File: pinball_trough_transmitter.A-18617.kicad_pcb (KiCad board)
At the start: 2 copper layers, 162.6 x 88.5 mm, 16 parts, among them J1 Conn_01x09_Male, J2 Conn_01x09_Male, Q1 SFH460, Q2 SFH460, Q3 SFH460, Q4 SFH460, Q5 SFH460, Q6 SFH460, Q7 SFH460

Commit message: Minor adjustments
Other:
- outline, holes or cut-outs redrawn
- board text added: "Rev: v1.13"
- board text removed: "Rev: v1.12"
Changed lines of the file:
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@@
   (general
     (thickness 1.6)
-    (drawings 31)
+    (drawings 39)
     (tracks 0)
     (zones 0)
@@
   (page A4)
   (title_block
-    (rev v1.12)
+    (rev v1.13)
   )
   (layers
@@
     )
   )
-  (gr_text "Rev: v1.12" (at 68.81 81.1) (layer F.SilkS)
+  (gr_line (start 210 45.72) (end 210 53.72) (layer Edge.Cuts) (width 0.15))
+  (gr_line (start 180 45.72) (end 180 53.72) (layer Edge.Cuts) (width 0.15))
+  (gr_line (start 130 45.72) (end 130 53.72) (layer Edge.Cuts) (width 0.15))
+  (gr_line (start 100 45.72) (end 100 53.72) (layer Edge.Cuts) (width 0.15))
+  (gr_line (start 130 45.72) (end 180 45.72) (layer Edge.Cuts) (width 0.15))
+  (gr_line (start 100 53.72) (end 130 53.72) (layer Edge.Cuts) (width 0.15))
+  (gr_line (start 180 53.72) (end 210 53.72) (layer Edge.Cuts) (width 0.15))
+  (gr_line (start 210 45.72) (end 229.87 45.72) (layer Edge.Cuts) (width 0.15))
+  (gr_text "Rev: v1.13" (at 68.81 81.1) (layer F.SilkS)
     (effects (font (size 1.5 1.5) (thickness 0.3)) (justify left))
   )
@@
   (gr_line (start 73.02 54.51) (end 73.02 62.13) (layer F.SilkS) (width 0.15))
   (gr_line (start 80.64 54.51) (end 73.02 54.51) (layer F.SilkS) (width 0.15))
-  (gr_circle (center 144.407 57.277) (end 145.894898 58.547) (layer Edge.Cuts) (width 0.15))
+  (gr_circle (center 144.907 57.277) (end 146.394898 58.547) (layer Edge.Cuts) (width 0.15))
   (gr_circle (center 90.424 57.785) (end 91.911898 59.055) (layer Edge.Cuts) (width 0.15))
-  (gr_circle (center 144.407 63.627) (end 145.894898 64.897) (layer Edge.Cuts) (width 0.15))
+  (gr_circle (center 144.907 63.627) (end 146.394898 64.897) (layer Edge.Cuts) (width 0.15))
   (gr_circle (center 199.144 69.85) (end 200.631898 71.12) (layer Edge.Cuts) (width 0.15))
   (gr_line (start 67.277387 134.230068) (end 229.837387 134.230068) (layer Edge.Cuts) (width 0.15))
@@
   (gr_line (start 229.87 59.69) (end 213.36 83.82) (layer Edge.Cuts) (width 0.15))
   (gr_line (start 229.87 45.72) (end 229.87 59.69) (layer Edge.Cuts) (width 0.15))
-  (gr_line (start 67.31 45.72) (end 229.87 45.72) (layer Edge.Cuts) (width 0.15))
+  (gr_line (start 67.31 45.72) (end 100 45.72) (layer Edge.Cuts) (width 0.15))
   (gr_line (start 67.31 83.82) (end 213.36 83.82) (layer Edge.Cuts) (width 0.15))
 )

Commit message: Final adjustments (hopefully)
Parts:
- removed J2: Conn_01x09_Male, Connector_Molex:Molex_KK-254_AE-6410-09A_1x09_P2.54mm_Vertical
- removed Q1, Q2, Q3, Q4, Q5, Q6, Q7: SFH460, LED_THT:LED_D5.0mm_IRBlack
- J1: footprint Connector_Molex:Molex_KK-254_AE-6410-09A_1x09_P2.54mm_Vertical -> Connector_PinHeader_2_54:PinHeader_1x09_P2.54mm_Horizontal
- moved J1 1.42 mm to (122.6, 75.6), turned to 270 degrees
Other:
- board size 162.6 x 88.5 mm -> 162.6 x 38.1 mm
- board text added: "Rev: v1.14"
- board text removed: "Rev: v1.13"

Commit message: Manually flip board
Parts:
- moved D1 444.5 mm to (-222.2, 55.7)
- moved D2 424.4 mm to (-212.2, 74.8)
- moved D3 370.2 mm to (-185.1, 71.8)
- moved D4 316.1 mm to (-158.0, 68.7)
- moved D5 262.0 mm to (-131.0, 65.7)
- moved J1 245.1 mm to (-122.6, 75.6)
- moved D6 207.8 mm to (-103.9, 62.6)
- moved D7 153.7 mm to (-76.8, 59.6)
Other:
- outline, holes or cut-outs redrawn
- board text added: "Rev: v1.15"
- board text removed: "Rev: v1.14"

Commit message: Programmatically flip instead
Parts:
- D1, D2, D3, D4, D5, D6, D7, J1: moved to B.Cu
- moved J1 292.5 mm to (168.9, 100.3)
- moved D1 292.3 mm to (69.2, 77.9)
- moved D2 292.3 mm to (79.3, 97.1)
- moved D3 292.3 mm to (106.4, 94.0)
- moved D4 292.3 mm to (133.4, 91.0)
- moved D5 292.3 mm to (160.5, 87.9)
- moved D6 292.3 mm to (187.6, 84.9)
- moved D7 292.3 mm to (214.6, 81.8)
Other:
- board text added: "Rev: v1.16"
- board text removed: "Rev: v1.15"

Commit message: Almost there
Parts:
- moved D1 149.5 mm to (218.4, 87.5)
- moved D7 141.9 mm to (73.0, 91.3)
- moved D2 129.4 mm to (208.4, 106.6)
- moved D6 88.0 mm to (100.1, 94.4)
- moved D3 75.6 mm to (181.3, 103.5)
- moved J1 71.1 mm to (98.4, 109.9)
- moved D5 34.7 mm to (127.2, 97.4)
- moved D4 22.9 mm to (154.2, 100.5)
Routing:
- net Net-(D1-Pad1): track 0.00 -> 187.3 mm
- net Net-(D1-Pad2): track 0.00 -> 119.6 mm
- net Net-(D2-Pad2): track 0.00 -> 102.4 mm
- net Net-(D3-Pad2): track 0.00 -> 77.5 mm
- net Net-(D4-Pad2): track 0.00 -> 52.1 mm
- net Net-(D7-Pad2): track 0.00 -> 35.1 mm
- net Net-(D5-Pad2): track 0.00 -> 28.9 mm
- net Net-(D6-Pad2): track 0.00 -> 13.3 mm
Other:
- outline, holes or cut-outs redrawn
- board text added: "(4 ball)"
- board text added: "(6 ball)"
- board text added: "(board)"
- board text added: "5768-14121-02"
- board text added: "A-18617"
- board text added: "A-18617-1"
- board text added: "BALL1"
- board text added: "BALL2"
- board text added: "BALL3"
- board text added: "BALL4"
- board text added: "BALL5"
- board text added: "BALL6"
- board text added: "COM"
- board text added: "COMPONENT SIDE"
- board text added: "JAM"
- board text added: "KEY"
- board text added: "Rev: v1.17"
- board text removed: "Rev: v1.16"

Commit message: I think... we're done
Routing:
- net Net-(D5-Pad2): track 28.9 -> 30.7 mm
- net Net-(D3-Pad2): track 77.5 -> 76.0 mm
- net Net-(D2-Pad2): track 102.4 -> 100.9 mm
- net Net-(D4-Pad2): track 52.1 -> 53.4 mm
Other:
- board text added: "4/6 Ball Opto Transmitter"
- board text added: "Rev: v1.18"
- board text removed: "Rev: v1.17"

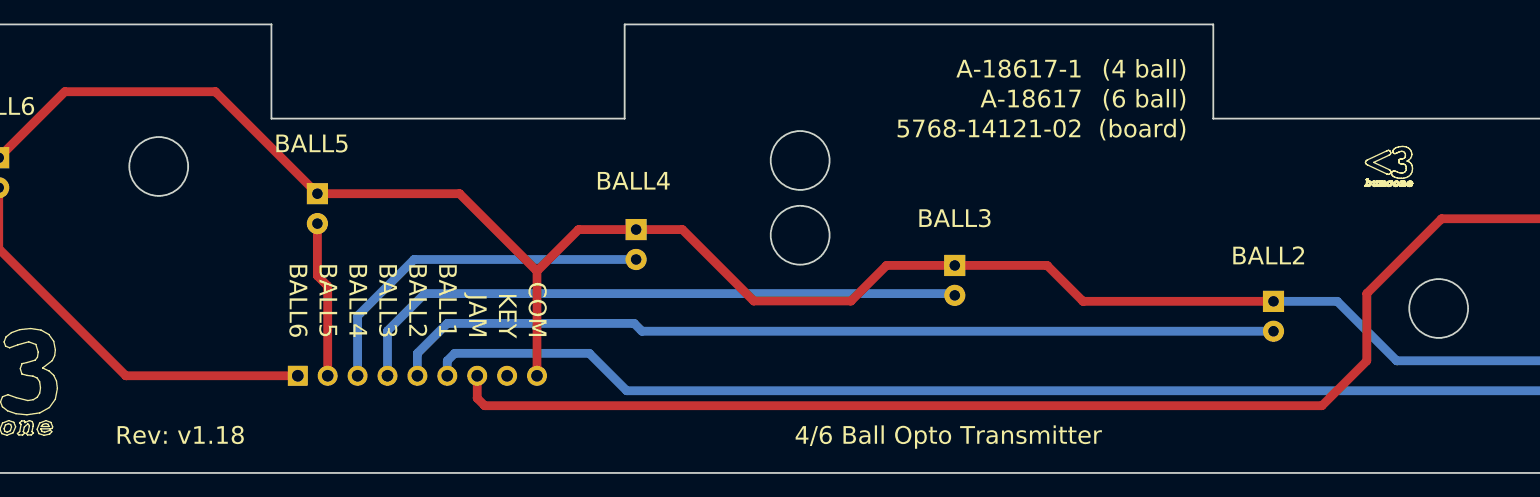
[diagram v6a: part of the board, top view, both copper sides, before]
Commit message: Move screw holes
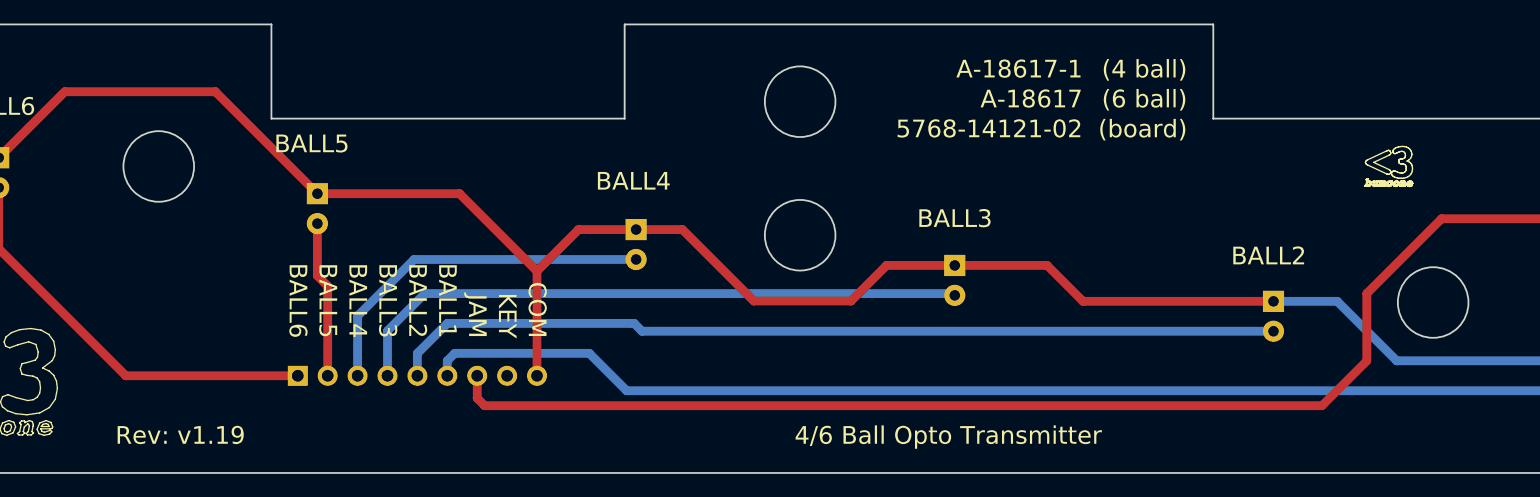
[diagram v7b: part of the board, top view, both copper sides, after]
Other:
- outline, holes or cut-outs redrawn
- board text added: "Rev: v1.19"
- board text removed: "Rev: v1.18"
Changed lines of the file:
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@@
   (page A4)
   (title_block
-    (rev v1.18)
+    (rev v1.19)
   )
   (layers
@@
   (gr_line (start 69.492244 107.223267) (end 68.579256 106.969267) (layer B.SilkS) (width 0.1))
   (gr_line (start 76.835 109.855) (end 76.454 110.107589) (layer B.SilkS) (width 0.1))
-  (gr_text "Rev: v1.18" (at 81.915 114.935) (layer B.SilkS)
+  (gr_text "Rev: v1.19" (at 81.915 114.935) (layer B.SilkS)
     (effects (font (size 1.5 1.5) (thickness 0.3)) (justify right mirror))
   )
@@
   (gr_line (start 191.22879 90.805726) (end 191.20687 90.773226) (layer F.SilkS) (width 0.05))
   (gr_line (start 191.17405 91.089906) (end 191.22093 91.047206) (layer F.SilkS) (width 0.05))
-  (gr_text "Rev: v1.18" (at 93.98 114.935) (layer F.SilkS)
+  (gr_text "Rev: v1.19" (at 93.98 114.935) (layer F.SilkS)
     (effects (font (size 1.5 1.5) (thickness 0.3)) (justify right))
   )
@@
   (gr_line (start 69.21 88.8) (end 69.21 96.42) (layer B.SilkS) (width 0.15))
   (gr_line (start 76.83 88.8) (end 69.21 88.8) (layer B.SilkS) (width 0.15))
-  (gr_circle (center 141.097 91.567) (end 143.597 91.567) (layer Edge.Cuts) (width 0.15))
-  (gr_circle (center 86.614 92.075) (end 89.114 92.075) (layer Edge.Cuts) (width 0.15))
-  (gr_circle (center 141.097 97.917) (end 143.597 97.917) (layer Edge.Cuts) (width 0.15))
-  (gr_circle (center 195.334 104.14) (end 197.834 104.14) (layer Edge.Cuts) (width 0.15))
+  (gr_circle (center 141.097 86.574) (end 144.097 86.574) (layer Edge.Cuts) (width 0.15))
+  (gr_circle (center 86.614 92.075) (end 89.614 92.075) (layer Edge.Cuts) (width 0.15))
+  (gr_circle (center 141.097 97.917) (end 144.097 97.917) (layer Edge.Cuts) (width 0.15))
+  (gr_circle (center 194.866 103.632) (end 197.866 103.632) (layer Edge.Cuts) (width 0.15))
   (gr_line (start 63.5 80.01) (end 63.5 118.11) (layer Edge.Cuts) (width 0.15))
   (gr_line (start 226.06 93.98) (end 209.55 118.11) (layer Edge.Cuts) (width 0.15))

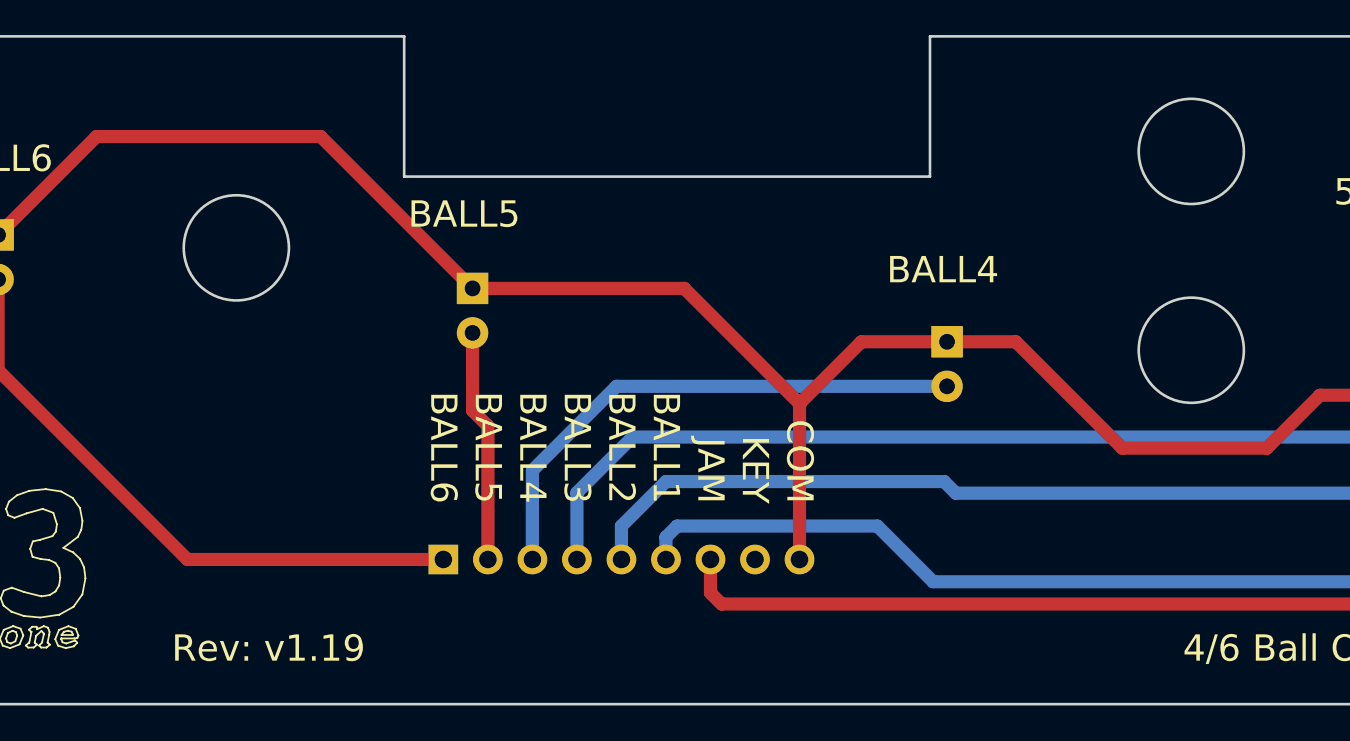
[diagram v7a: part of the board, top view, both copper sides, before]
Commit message: More screw hole adjustment
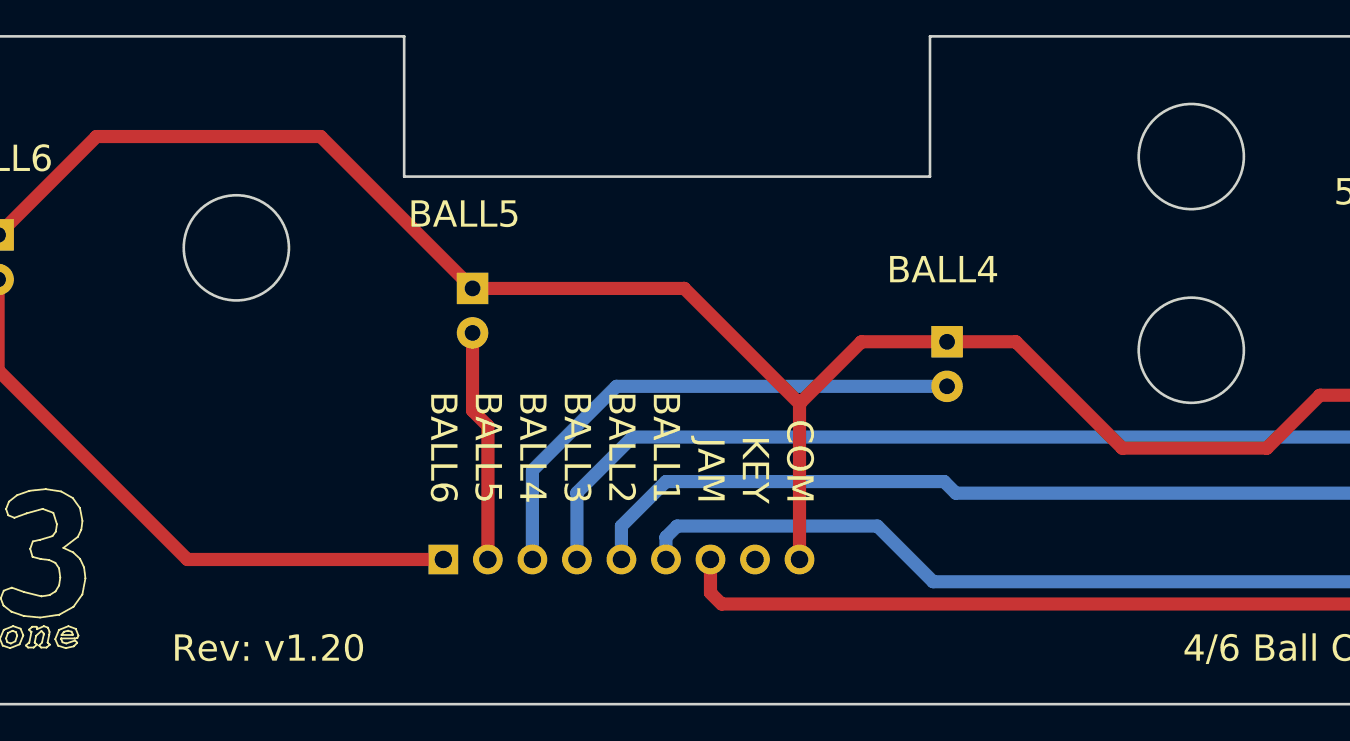
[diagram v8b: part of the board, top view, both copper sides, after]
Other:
- outline, holes or cut-outs redrawn
- board text added: "Rev: v1.20"
- board text removed: "Rev: v1.19"
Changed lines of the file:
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@@
   (page A4)
   (title_block
-    (rev v1.19)
+    (rev v1.20)
   )
   (layers
@@
   (gr_line (start 69.492244 107.223267) (end 68.579256 106.969267) (layer B.SilkS) (width 0.1))
   (gr_line (start 76.835 109.855) (end 76.454 110.107589) (layer B.SilkS) (width 0.1))
-  (gr_text "Rev: v1.19" (at 81.915 114.935) (layer B.SilkS)
+  (gr_text "Rev: v1.20" (at 81.915 114.935) (layer B.SilkS)
     (effects (font (size 1.5 1.5) (thickness 0.3)) (justify right mirror))
   )
@@
   (gr_line (start 191.22879 90.805726) (end 191.20687 90.773226) (layer F.SilkS) (width 0.05))
   (gr_line (start 191.17405 91.089906) (end 191.22093 91.047206) (layer F.SilkS) (width 0.05))
-  (gr_text "Rev: v1.19" (at 93.98 114.935) (layer F.SilkS)
+  (gr_text "Rev: v1.20" (at 93.98 114.935) (layer F.SilkS)
     (effects (font (size 1.5 1.5) (thickness 0.3)) (justify right))
   )
@@
   (gr_line (start 69.21 88.8) (end 69.21 96.42) (layer B.SilkS) (width 0.15))
   (gr_line (start 76.83 88.8) (end 69.21 88.8) (layer B.SilkS) (width 0.15))
-  (gr_circle (center 141.097 86.574) (end 144.097 86.574) (layer Edge.Cuts) (width 0.15))
+  (gr_circle (center 141.097 86.868) (end 144.097 86.868) (layer Edge.Cuts) (width 0.15))
   (gr_circle (center 86.614 92.075) (end 89.614 92.075) (layer Edge.Cuts) (width 0.15))
   (gr_circle (center 141.097 97.917) (end 144.097 97.917) (layer Edge.Cuts) (width 0.15))
